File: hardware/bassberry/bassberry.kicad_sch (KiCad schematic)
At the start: 0 parts

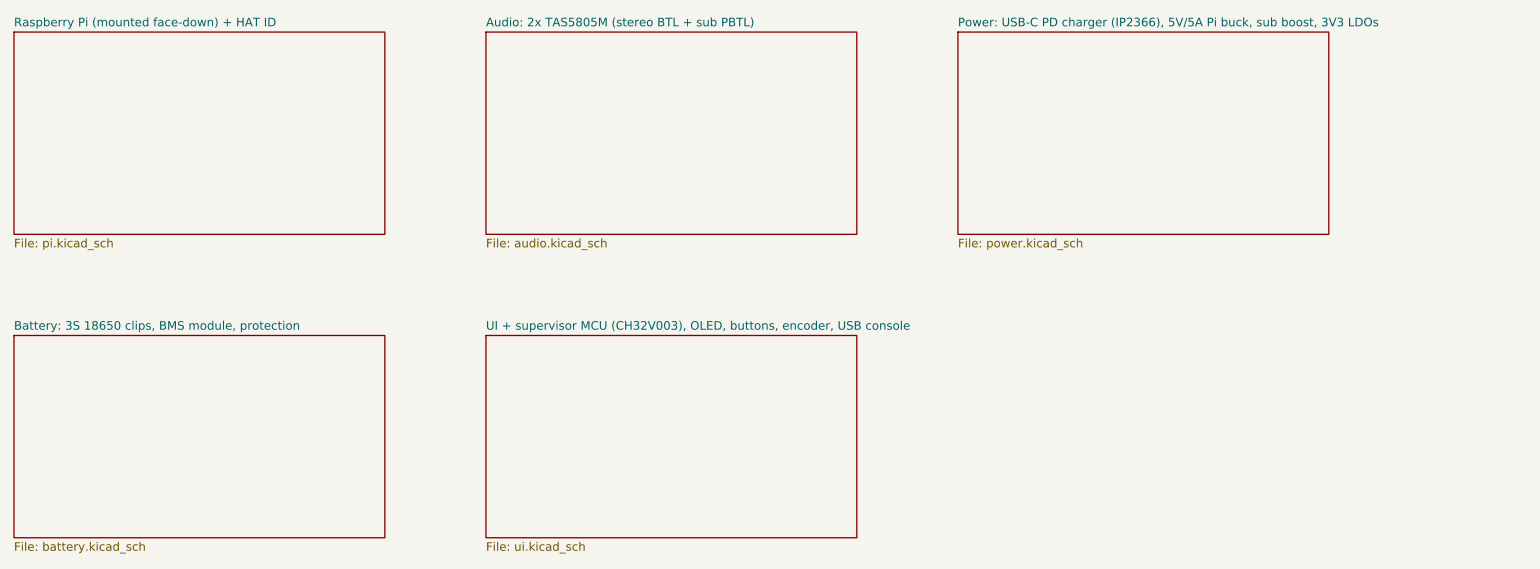
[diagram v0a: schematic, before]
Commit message: rev 0.2 board: routed with srouter, DRC 0 errors / 0 unconnected / 0 parity, digital twin 1-4 PASS; KiCad files, reports, renders
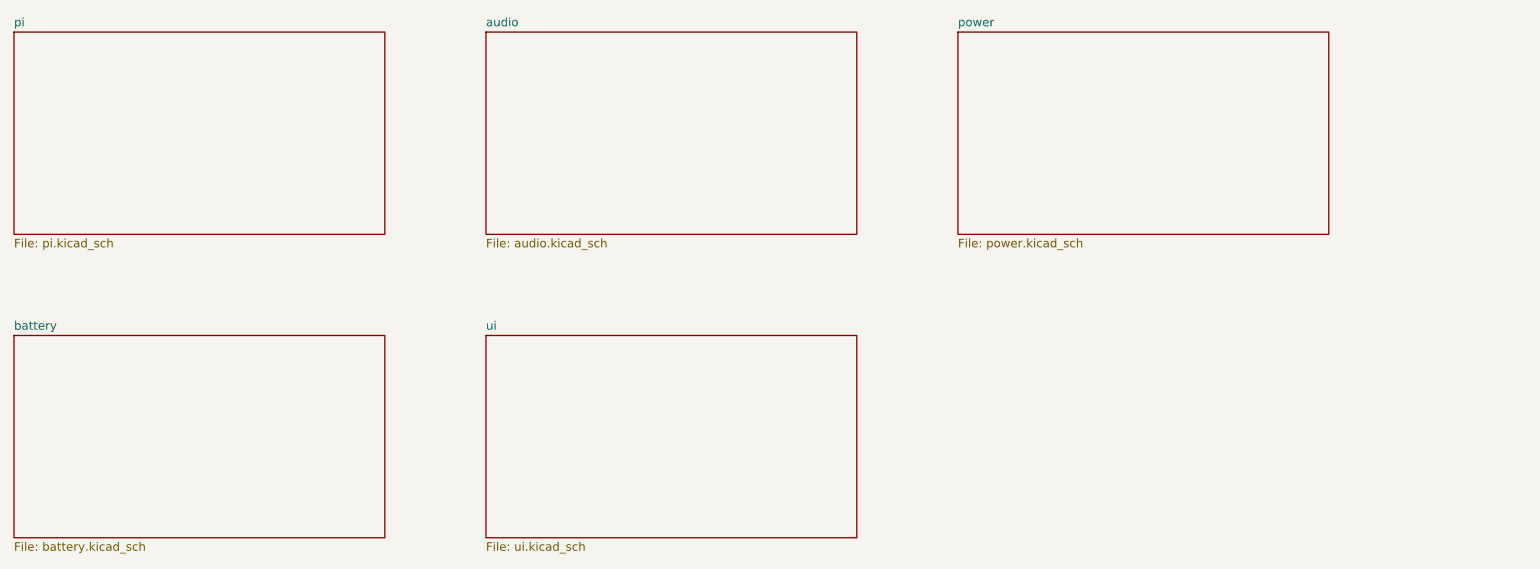
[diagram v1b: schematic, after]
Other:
- sheet Audio: 2x TAS5805M (stereo BTL + sub PBTL) renamed audio
- sheet Battery: 3S 18650 clips, BMS module, protection renamed battery
- sheet Power: USB-C PD charger (IP2366), 5V/5A Pi buck, sub boost, 3V3 LDOs renamed power
- sheet Raspberry Pi (mounted face-down) + HAT ID renamed pi
- sheet UI + supervisor MCU (CH32V003), OLED, buttons, encoder, USB console renamed ui
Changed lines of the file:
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@@
 			(color 0 0 0 0)
 		)
-		(property "Sheetname" "Raspberry Pi (mounted face-down) + HAT ID"
+		(property "Sheetname" "pi"
 			(at 30 39.3 0)
 			(effects
@@
 			(color 0 0 0 0)
 		)
-		(property "Sheetname" "Audio: 2x TAS5805M (stereo BTL + sub PBTL)"
+		(property "Sheetname" "audio"
 			(at 100 39.3 0)
 			(effects
@@
 			(color 0 0 0 0)
 		)
-		(property "Sheetname" "Power: USB-C PD charger (IP2366), 5V/5A Pi buck, sub boost, 3V3 LDOs"
+		(property "Sheetname" "power"
 			(at 170 39.3 0)
 			(effects
@@
 			(color 0 0 0 0)
 		)
-		(property "Sheetname" "Battery: 3S 18650 clips, BMS module, protection"
+		(property "Sheetname" "battery"
 			(at 30 84.3 0)
 			(effects
@@
 			(color 0 0 0 0)
 		)
-		(property "Sheetname" "UI + supervisor MCU (CH32V003), OLED, buttons, encoder, USB console"
+		(property "Sheetname" "ui"
 			(at 100 84.3 0)
 			(effects
